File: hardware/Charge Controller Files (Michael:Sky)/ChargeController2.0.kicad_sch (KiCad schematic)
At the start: 90 parts, among them J1 GND_TEST_01x01_Pin, J10 SOL_TEST_01x01_Pin, J13 Conn-1x2, J14 Conn-1x2, J15 Conn-1x2, J17 SCL_MAS_01x01_Pin, J18 SDA_MAS_01x01_Pin, J19 SYS-1x2, J2 SP_01x02_Pin, J3 BATT_TEST_01x01_Pin, J4 3.3V_PULLUP_01x02_Pin, J5 BATT_01x02_Pin, J6 Conn-1x2, J7 Conn-1x2, J8 Conn-1x2, J9 SYS_TEST_01x01_Pin, Q1 SI2318DS-T1-E3, Q10 SI2318DS-T1-E3, Q11 SI2318DS-T1-E3, Q12 SI2318DS-T1-E3, Q2 SI2318DS-T1-E3, Q3 SI2318DS-T1-E3, Q4 SI2318DS-T1-E3, Q5 AONS66614, Q6 AONS66614, Q7 AONS66614, Q8 AONS66614, Q9 SI2318DS-T1-E3, SW1 100SP1T1B1M1QEH, U1 BQ25756ERRVR

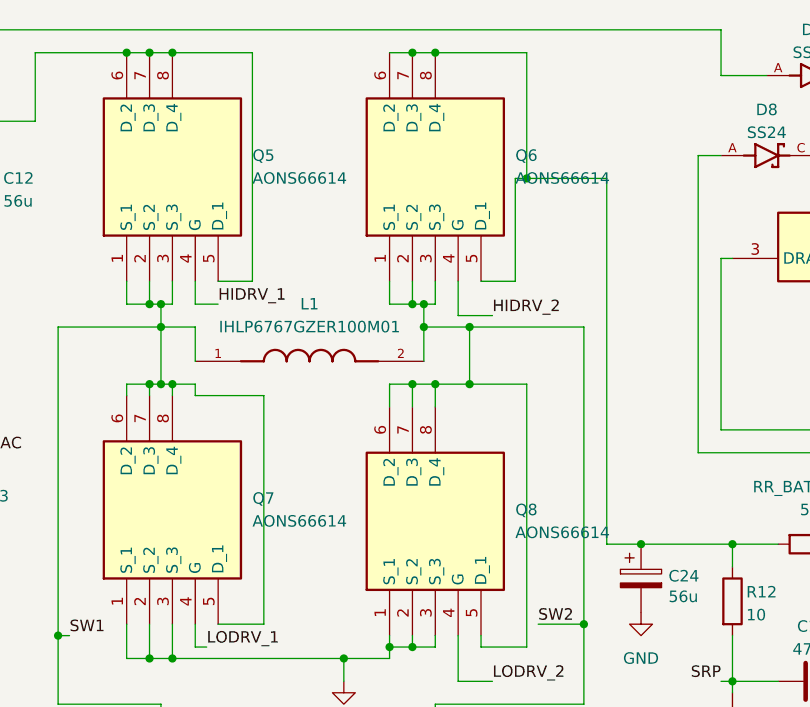
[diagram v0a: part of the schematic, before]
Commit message: PCB routing/MOSFET fix
- PCB routing
- MOSFET footprint fix (9 pins)
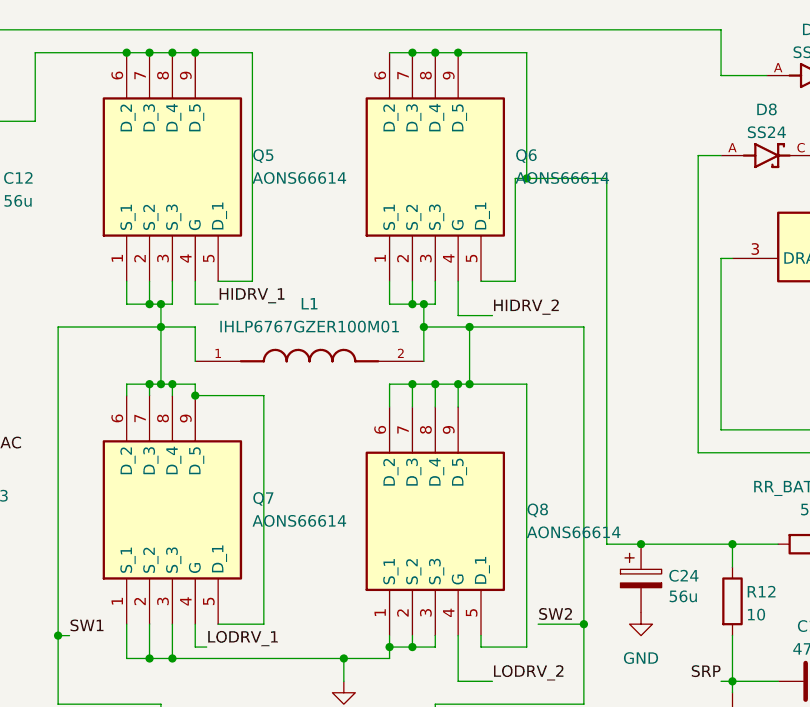
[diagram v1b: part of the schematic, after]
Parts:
- Q5, Q6, Q7, Q8: Arrow Part Number AONS66614 -> (none); Arrow Price/Stock https://www.arrow.com/en/products/aons66614/alpha-and-omega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 -> (none)
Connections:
- net SW1: now also Q7.9 (D_5)
- net SW2: now also Q8.9 (D_5)
- net at C24.1, Q6.5 (D_1), Q6.6 (D_2)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: now also Q6.9 (D_5)
- net at C12.1, Q5.5 (D_1), Q5.6 (D_2)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: now also Q5.9 (D_5)

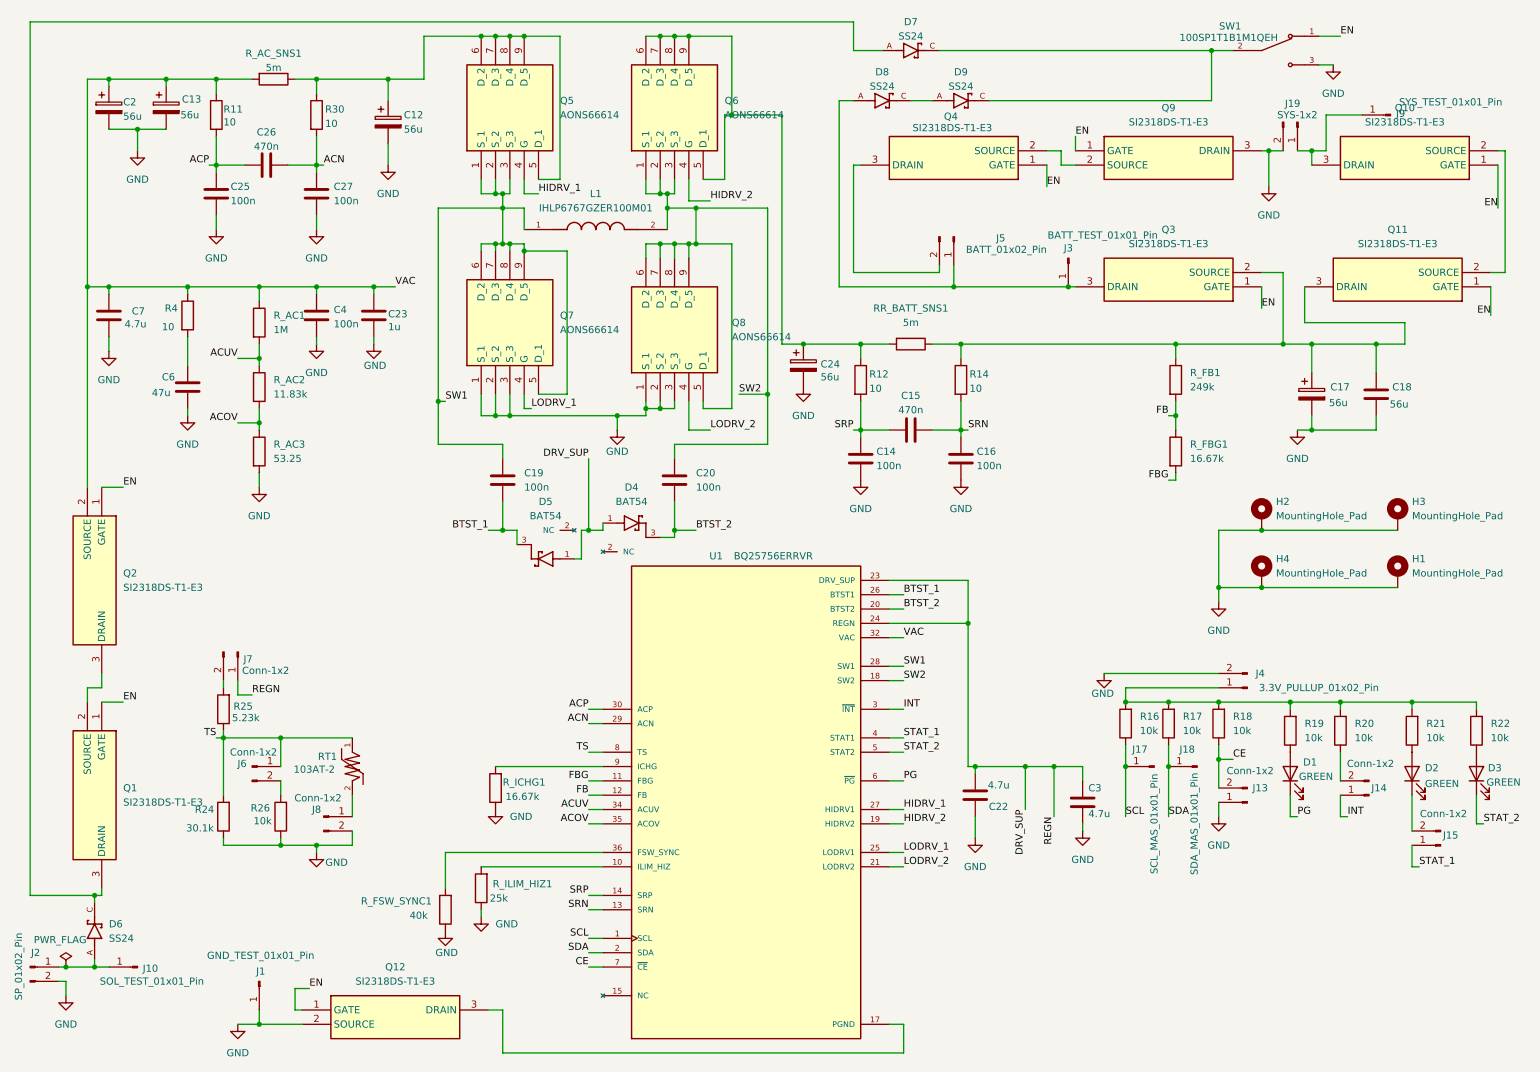
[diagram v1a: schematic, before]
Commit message: PCB fixes
Changed RAC_3 symbol and footprint, changed Inhibits mosfets to later (better) version.
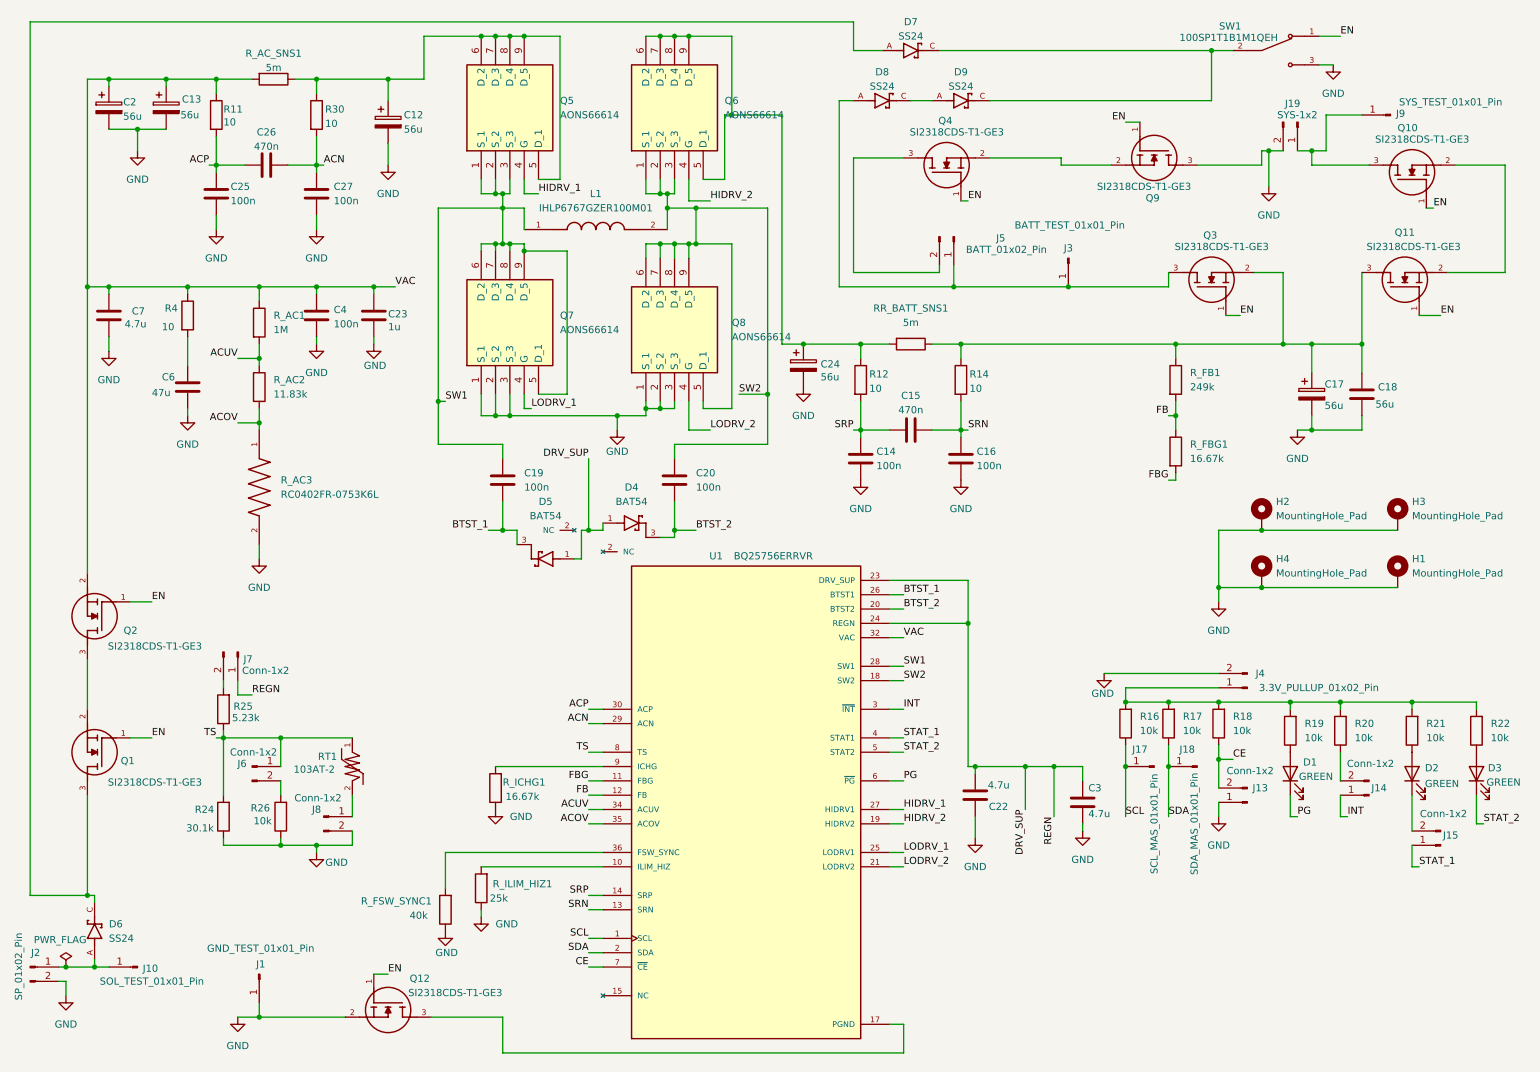
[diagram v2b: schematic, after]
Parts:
- removed Q1, Q10, Q11, Q12, Q2, Q3, Q4, Q9: SI2318DS-T1-E3, bmsfootprints:SI2318DS-T1-E3, symbol SI2318DS-T1-E3:SI2318DS-T1-E3
- removed R_AC3: 53.25, Resistor_SMD:R_1206_3216Metric, symbol Device:R
- added Q1, Q10, Q11, Q12, Q2, Q3, Q4, Q9: SI2318CDS-T1-GE3, bmsfootprints:SI2318CDS-T1-GE3, symbol SI2318CDS-T1-GE3:SI2318CDS-T1-GE3
- added R_AC3: RC0402FR-0753K6L, bmsfootprints:RC0402FR-0753K6L, symbol RC0402FR-0753K6L:RC0402FR-0753K6L
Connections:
- net ACOV: now also R_AC3.1
- net EN: now also Q1.1, Q10.1, Q11.1, Q12.1, Q2.1, Q3.1, Q4.1, Q9.1
- net GND: now also Q12.2, Q9.3, R_AC3.2
- net PGND: now also Q12.3
- net VAC: now also Q2.2
- net at D6.C, D7.A: now also Q1.3
- net at J19.1 (Pin_1), J9.1 (Pin_1): now also Q10.3
- net at C17.1, C18.1, R14.1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: now also Q11.3, Q3.2
- net at D8.A, J3.1 (Pin_1), J5.1 (Pin_1): now also Q3.3
- net at J5.2 (Pin_2): now also Q4.3
- new net: Q10.2, Q11.2
- new net: Q1.2, Q2.3
- new net: Q4.2, Q9.2
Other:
- moved on the sheet: C18, J1

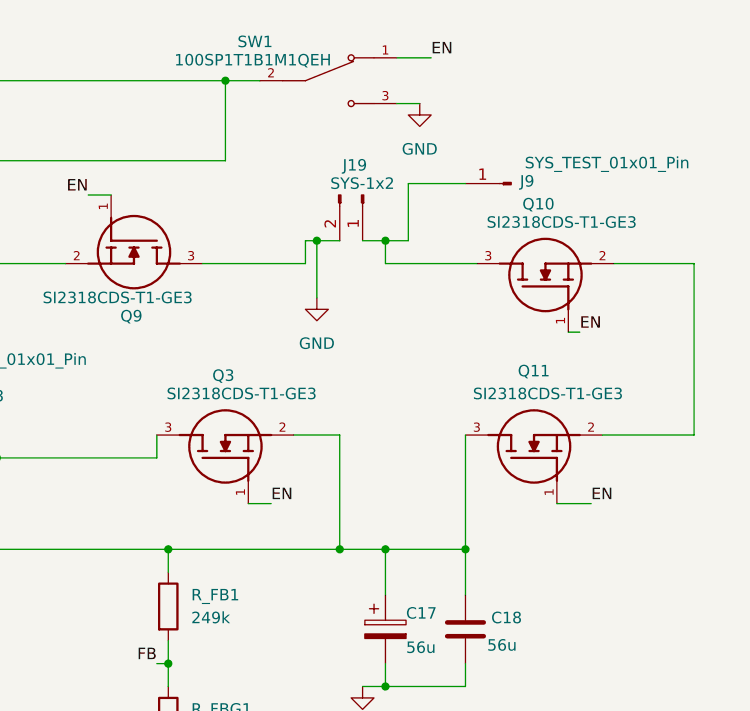
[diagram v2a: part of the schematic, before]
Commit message: Update ChargeController2.0.kicad_sch
pcb addition
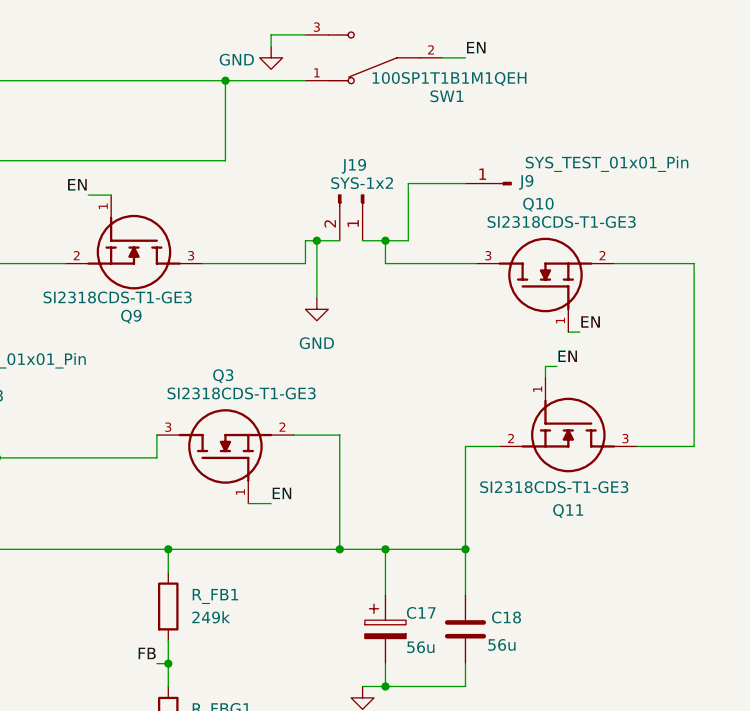
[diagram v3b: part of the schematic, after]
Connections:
- net EN: now also SW1.2; no longer SW1.1
- net at D7.C, D9.C: now also SW1.1; no longer SW1.2
- net at C17.1, C18.1, Q3.2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: now also Q11.2; no longer Q11.3
- net at Q10.2: now also Q11.3; no longer Q11.2
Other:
- moved on the sheet: Q11, SW1

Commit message: Ready for Manufacturing
Final push
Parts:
- removed D6: SS24, bmsfootprints:SS24, symbol SS24:SS24
- removed Q12: SI2318CDS-T1-GE3, bmsfootprints:SI2318CDS-T1-GE3, symbol SI2318CDS-T1-GE3:SI2318CDS-T1-GE3
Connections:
- net PGND is gone; now on net GND: U1.17 (PGND), U1.22 (PGND), U1.37 (PGND)
- net at C17.1, C18.1, Q3.2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: now also Q11.3; no longer Q11.2
- net at D7.A, Q1.3: now also J10.1 (Pin_1), J2.1 (Pin_1)
- net at J19.1 (Pin_1), J9.1 (Pin_1): now also Q10.2; no longer Q10.3
- new net: Q10.3, Q11.2
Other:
- moved on the sheet: J6, J7, J8, Q10, Q11, R24, R25, R26, RT1
